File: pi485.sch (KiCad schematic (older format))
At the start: 27 parts, among them J1 RS485, P1 Rasperry Pi, P2 PWR, P3 Term, P4 Latch Disable, Q1 2N4401, Q2 2N4401, Q3 2N4401, U1 NE555, U2 MAX485

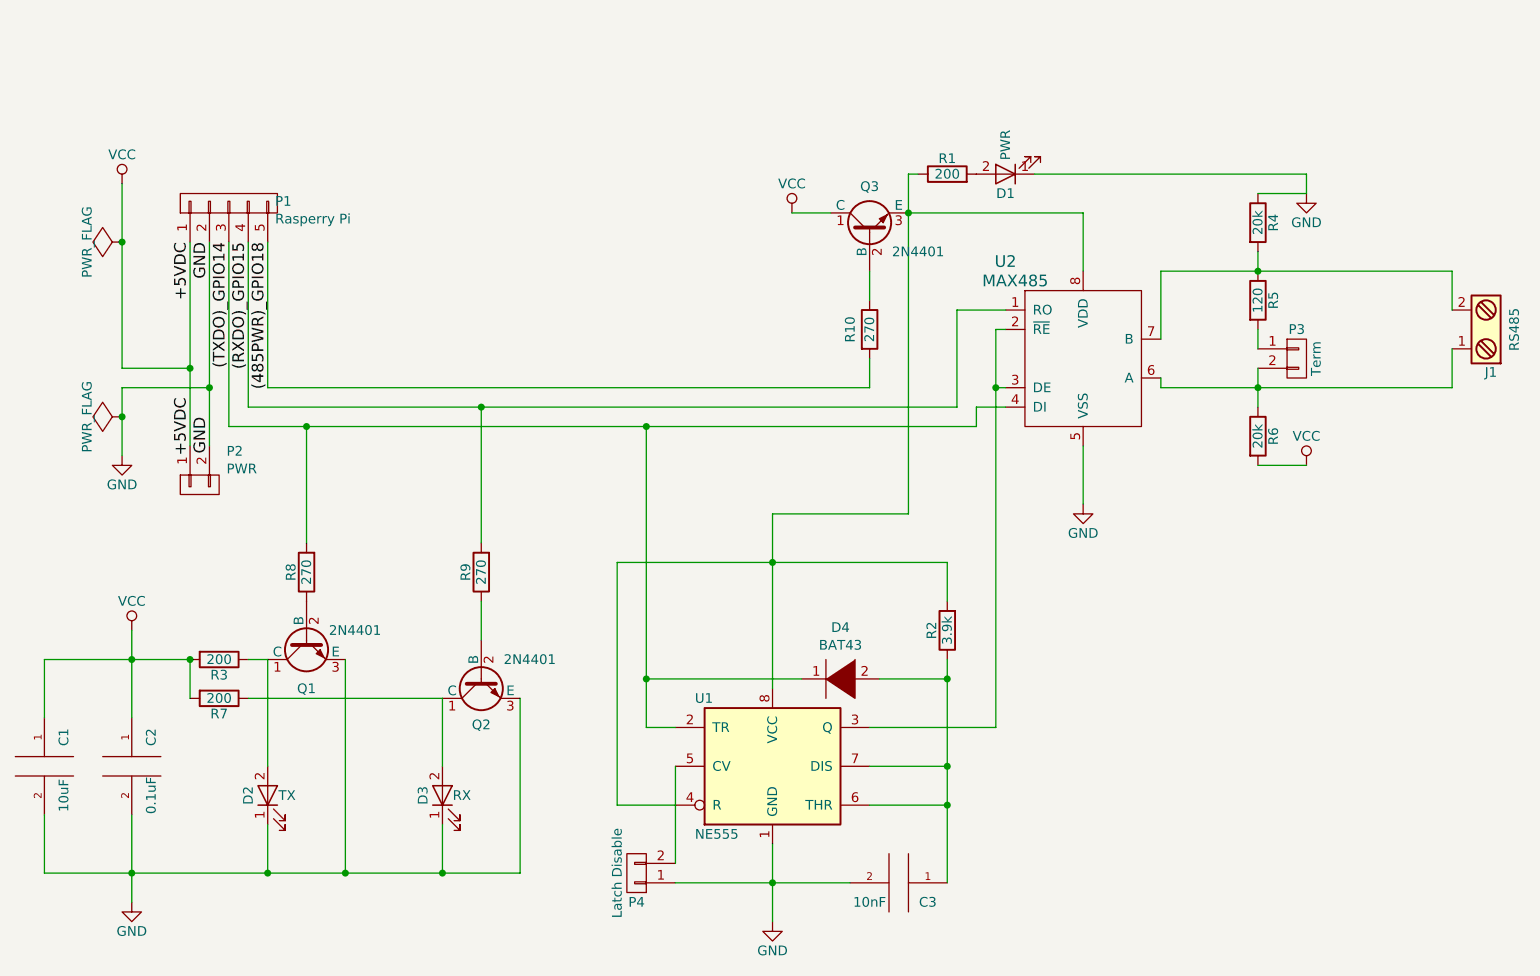
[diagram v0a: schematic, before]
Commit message: * Added 3.3v enable / disable pin. Can be tied to 3.3v output on the pi, or a GPIO pin to force power off / on of the pi485 circuits. * Enables software control of a RS485 'reset', and will make it easier to support using LC-Tech 'carrier' boards in an alternate layout.
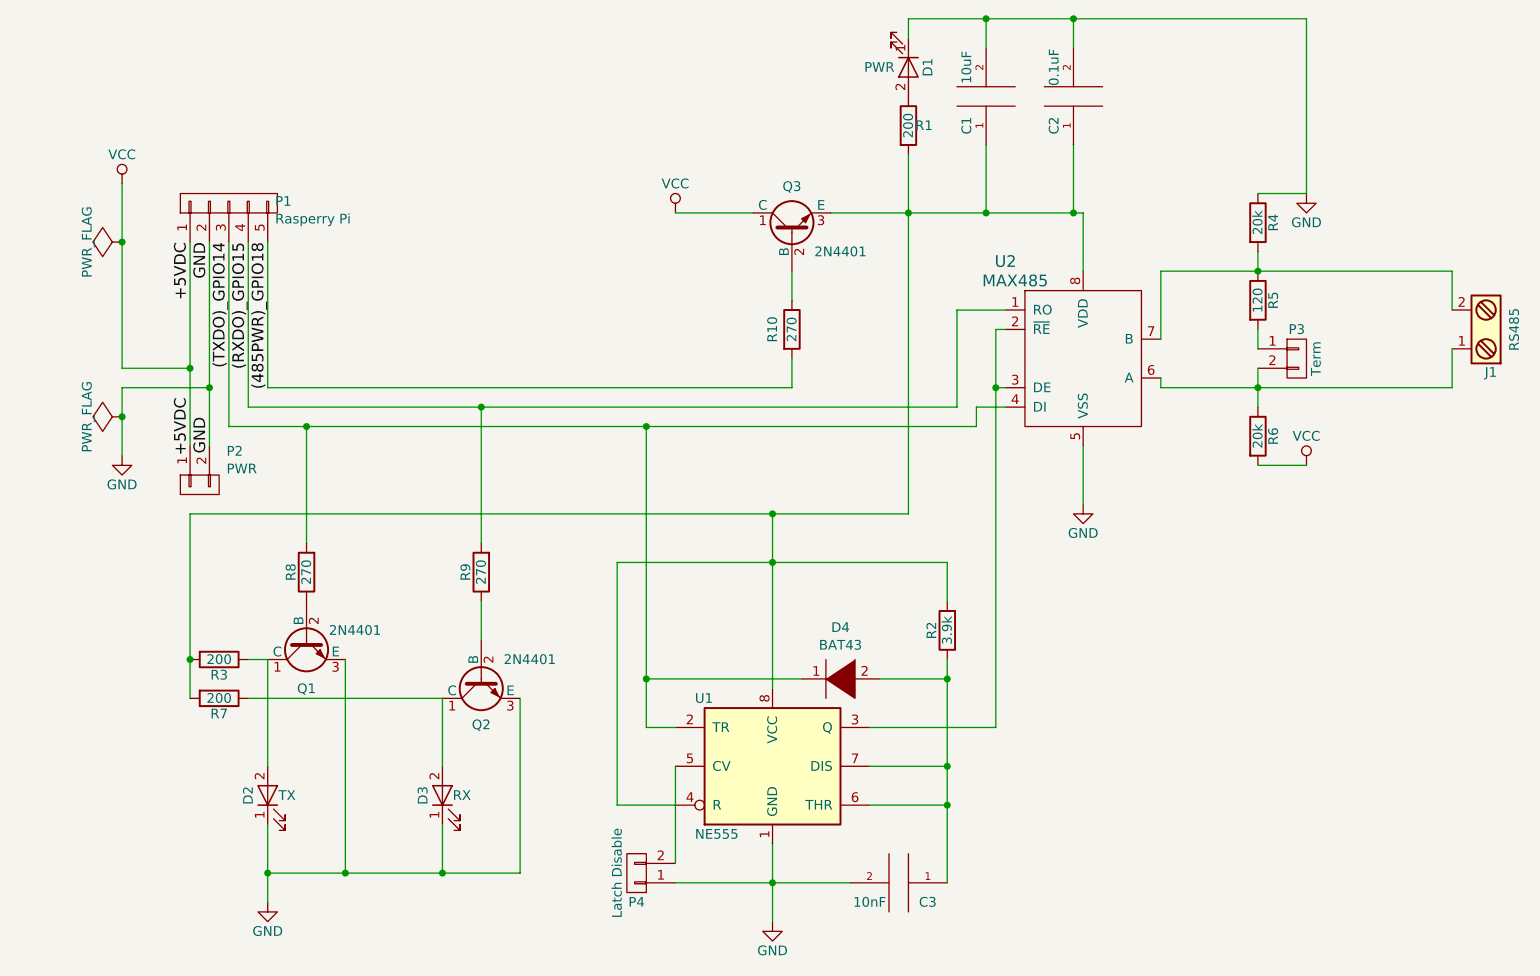
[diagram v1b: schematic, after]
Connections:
- net VCC: no longer C1.1, C2.1, R3.2, R7.2
- net at Q3.3 (E), R2.2, U1.4 (R)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: now also C1.1, C2.1, R1.2, R3.2, R7.2; no longer R1.1
- net at D1.2 (A): now also R1.1; no longer R1.2
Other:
- moved on the sheet: C1, C2, D1, Q3, R1, R10
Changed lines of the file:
@@
-$EndComp
-$Comp
-L VCC #PWR05
-U 1 1 586E8496
-P 2200 4150
-F 0 "#PWR05" H 2200 4000 50  0001 C CNN
-F 1 "VCC" H 2200 4300 50  0000 C CNN
-F 2 "" H 2200 4150 50  0000 C CNN
-F 3 "" H 2200 4150 50  0000 C CNN
-	1    2200 4150
-	1    0    0    -1
 $EndComp
 $Comp
 L GND #PWR06
 U 1 1 586E84AD
-P 2200 5550
-F 0 "#PWR06" H 2200 5300 50  0001 C CNN
-F 1 "GND" H 2200 5400 50  0000 C CNN
-F 2 "" H 2200 5550 50  0000 C CNN
-F 3 "" H 2200 5550 50  0000 C CNN
-	1    2200 5550
+P 2900 5550
+F 0 "#PWR06" H 2900 5300 50  0001 C CNN
+F 1 "GND" H 2900 5400 50  0000 C CNN
+F 2 "" H 2900 5550 50  0000 C CNN
+F 3 "" H 2900 5550 50  0000 C CNN
+	1    2900 5550
 	1    0    0    -1
 $EndComp
@@
 L R R1
 U 1 1 586E84C4
-P 6400 1800
-F 0 "R1" V 6480 1800 50  0000 C CNN
-F 1 "200" V 6400 1800 50  0000 C CNN
-F 2 "Resistors_THT:Resistor_Horizontal_RM10mm" V 6550 1100 50  0001 C CNN
-F 3 "" H 6400 1800 50  0000 C CNN
-	1    6400 1800
-	0    -1   -1   0
+P 6200 1550
+F 0 "R1" H 6280 1550 50  0000 C CNN
+F 1 "200" V 6200 1550 50  0000 C CNN
+F 2 "Resistors_THT:Resistor_Horizontal_RM10mm" V 6350 850 50  0001 C CNN
+F 3 "" H 6200 1550 50  0000 C CNN
+	1    6200 1550
+	1    0    0    -1
 $EndComp
 $Comp
 L LED D1
 U 1 1 586E8531
-P 6700 1800
-F 0 "D1" H 6700 1900 50  0000 C CNN
-F 1 "PWR" V 6700 1650 50  0000 C CNN
-F 2 "LEDs:LED-3MM" H 6650 1600 50  0001 C CNN
-F 3 "" H 6700 1800 50  0000 C CNN
-	1    6700 1800
-	-1   0    0    1
+P 6200 1250
+F 0 "D1" H 6200 1350 50  0000 C CNN
+F 1 "PWR" V 6200 1100 50  0000 C CNN
+F 2 "LEDs:LED-3MM" H 6150 1050 50  0001 C CNN
+F 3 "" H 6200 1250 50  0000 C CNN
+	1    6200 1250
+	0    1    1    0
 $EndComp
 $Comp
@@
 $EndComp
 $Comp
-L GND #PWR09
+L GND #PWR08
 U 1 1 586EB44F
 P 7100 3500
-F 0 "#PWR09" H 7100 3250 50  0001 C CNN
+F 0 "#PWR08" H 7100 3250 50  0001 C CNN
 F 1 "GND" H 7100 3350 50  0000 C CNN
 F 2 "" H 7100 3500 50  0000 C CNN
@@
 $EndComp
 $Comp
-L VCC #PWR010
+L VCC #PWR09
 U 1 1 586EB484
-P 5600 2000
-F 0 "#PWR010" H 5600 1850 50  0001 C CNN
-F 1 "VCC" H 5600 2150 50  0000 C CNN
-F 2 "" H 5600 2000 50  0000 C CNN
-F 3 "" H 5600 2000 50  0000 C CNN
-	1    5600 2000
+P 5000 2000
+F 0 "#PWR09" H 5000 1850 50  0001 C CNN
+F 1 "VCC" H 5000 2150 50  0000 C CNN
+F 2 "" H 5000 2000 50  0000 C CNN
+F 3 "" H 5000 2000 50  0000 C CNN
+	1    5000 2000
 	1    0    0    -1
 $EndComp
@@
 GND
 $Comp
-L GND #PWR011
+L GND #PWR010
 U 1 1 586F0172
 P 8250 1900
-F 0 "#PWR011" H 8250 1650 50  0001 C CNN
+F 0 "#PWR010" H 8250 1650 50  0001 C CNN
 F 1 "GND" H 8250 1750 50  0000 C CNN
 F 2 "" H 8250 1900 50  0000 C CNN
@@
 $EndComp
 $Comp
-L VCC #PWR012
+L VCC #PWR011
 U 1 1 586F01EA
 P 8250 3300
-F 0 "#PWR012" H 8250 3150 50  0001 C CNN
+F 0 "#PWR011" H 8250 3150 50  0001 C CNN
 F 1 "VCC" H 8250 3450 50  0000 C CNN
 F 2 "" H 8250 3300 50  0000 C CNN
@@
 L CAP C2
 U 1 1 5876F3DF
-P 2200 4850
-F 0 "C2" V 2300 5000 50  0000 C CNN
-F 1 "0.1uF" V 2300 4700 50  0000 C CNN
-F 2 "Capacitors_THT:C_Rect_L7_W2.5_P5" V 2400 4550 50  0001 C CNN
-F 3 "" H 2200 4850 50  0000 C CNN
-	1    2200 4850
-	1    0    0    -1
+P 7050 1400
+F 0 "C2" V 7150 1550 50  0000 C CNN
+F 1 "0.1uF" V 7150 1250 50  0000 C CNN
+F 2 "Capacitors_THT:C_Rect_L7_W2.5_P5" V 7250 1100 50  0001 C CNN
+F 3 "" H 7050 1400 50  0000 C CNN
+	1    7050 1400
+	-1   0    0    1
 $EndComp
 $Comp
 L CAP C1
 U 1 1 5876F5F2
-P 1750 4850
-F 0 "C1" V 1850 5000 50  0000 C CNN
-F 1 "10uF" V 1850 4700 50  0000 C CNN
-F 2 "Capacitors_THT:C_Radial_D5_L11_P2" V 1950 4550 50  0001 C CNN
-F 3 "" H 1750 4850 50  0000 C CNN
-	1    1750 4850
-	1    0    0    -1
+P 6600 1400
+F 0 "C1" V 6700 1550 50  0000 C CNN
+F 1 "10uF" V 6700 1250 50  0000 C CNN
+F 2 "Capacitors_THT:C_Radial_D5_L11_P2" V 6800 1100 50  0001 C CNN
+F 3 "" H 6600 1400 50  0000 C CNN
+	1    6600 1400
+	-1   0    0    1
 $EndComp
 $Comp
@@
 L R R10
 U 1 1 587FCED5
-P 6000 2600
-F 0 "R10" V 5900 2600 50  0000 C CNN
-F 1 "270" V 6000 2600 50  0000 C CNN
-F 2 "Resistors_THT:Resistor_Horizontal_RM10mm" V 6150 1900 50  0001 C CNN
-F 3 "" H 6000 2600 50  0000 C CNN
-	1    6000 2600
+P 5600 2600
+F 0 "R10" V 5500 2600 50  0000 C CNN
+F 1 "270" V 5600 2600 50  0000 C CNN
+F 2 "Resistors_THT:Resistor_Horizontal_RM10mm" V 5750 1900 50  0001 C CNN
+F 3 "" H 5600 2600 50  0000 C CNN
+	1    5600 2600
 	1    0    0    -1
 $EndComp
@@
 L BC413 Q3
 U 1 1 587FCF77
-P 6000 2100
-F 0 "Q3" V 6236 2100 50  0000 C CNN
-F 1 "2N4401" V 5900 1850 50  0000 C CNN
-F 2 "TO_SOT_Packages_THT:TO-92_Inline_Wide" V 6418 2100 50  0001 C CIN
-F 3 "" H 6000 2100 50  0000 L CNN
-	1    6000 2100
+P 5600 2100
+F 0 "Q3" V 5836 2100 50  0000 C CNN
+F 1 "2N4401" V 5500 1850 50  0000 C CNN
+F 2 "TO_SOT_Packages_THT:TO-92_Inline_Wide" V 6018 2100 50  0001 C CIN
+F 3 "" H 5600 2100 50  0000 L CNN
+	1    5600 2100
 	0    -1   -1   0
 $EndComp
@@
 Wire Wire Line
 	2600 2900 2150 2900
-Wire Wire Line
-	1750 4300 2500 4300
 Wire Wire Line
 	5500 3550 5500 4450
@@
 	8000 3300 8250 3300
 Wire Wire Line
-	8000 1900 8250 1900
+	8250 1900 8000 1900
 Wire Wire Line
 	8000 2600 8000 2700
@@
 	2900 4300 2900 4850
 Wire Wire Line
-	1750 5400 4200 5400
-Wire Wire Line
-	2900 5150 2900 5400
-Connection ~ 2200 4300
+	2900 5150 2900 5550
 Wire Wire Line
 	2800 4300 2900 4300
 Wire Wire Line
-	2500 4300 2500 4500
+	2500 3550 2500 4500
 Wire Wire Line
 	2800 4500 3800 4500
@@
 Connection ~ 4000 3000
 Wire Wire Line
-	2200 5100 2200 5550
-Connection ~ 2200 5400
-Wire Wire Line
-	1750 4600 1750 4300
-Wire Wire Line
-	1750 5100 1750 5400
-Wire Wire Line
-	2200 4150 2200 4600
-Wire Wire Line
 	6050 4400 6400 4400
 Connection ~ 6400 5050
 Wire Wire Line
 	5000 5350 5000 4850
-Wire Wire Line
-	6000 2450 6000 2300
-Wire Wire Line
-	5600 2000 5800 2000
 Text Label 2900 2150 3    60   ~ 0
 (485PWR)_GPIO18
@@
 	2900 2150 2900 2900
 Wire Wire Line
-	2900 2900 6000 2900
-Wire Wire Line
-	6000 2900 6000 2750
-Wire Wire Line
-	6200 2000 7100 2000
+	2900 2900 5600 2900
+Wire Wire Line
+	5600 2900 5600 2750
+Wire Wire Line
+	5800 2000 7100 2000
 Wire Wire Line
 	7100 2000 7100 2300
 Wire Wire Line
-	6250 1800 6200 1800
-Wire Wire Line
-	6200 1800 6200 3550
-Wire Wire Line
-	6850 1800 8250 1800
-Wire Wire Line
-	8250 1800 8250 1900
+	6200 3550 6200 1700
+Wire Wire Line
+	8250 1000 8250 1900
 Connection ~ 6200 2000
 Wire Wire Line
-	6200 3550 5500 3550
+	2500 3550 6200 3550
+Wire Wire Line
+	6200 1000 8250 1000
+Wire Wire Line
+	6200 1000 6200 1100
+Wire Wire Line
+	2900 5400 4200 5400
+Wire Wire Line
+	6600 2000 6600 1650
+Wire Wire Line
+	7050 1650 7050 2000
+Connection ~ 7050 2000
+Wire Wire Line
+	7050 1150 7050 1000
+Connection ~ 7050 1000
+Wire Wire Line
+	6600 1150 6600 1000
+Connection ~ 6600 1000
+Connection ~ 6600 2000
+Wire Wire Line
+	5000 2000 5400 2000
+Wire Wire Line
+	5600 2300 5600 2450
+Connection ~ 5500 3550
 $EndSCHEMATC
